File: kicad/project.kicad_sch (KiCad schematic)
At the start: 1 part, among them U1 ESP32-C3-WROOM-02

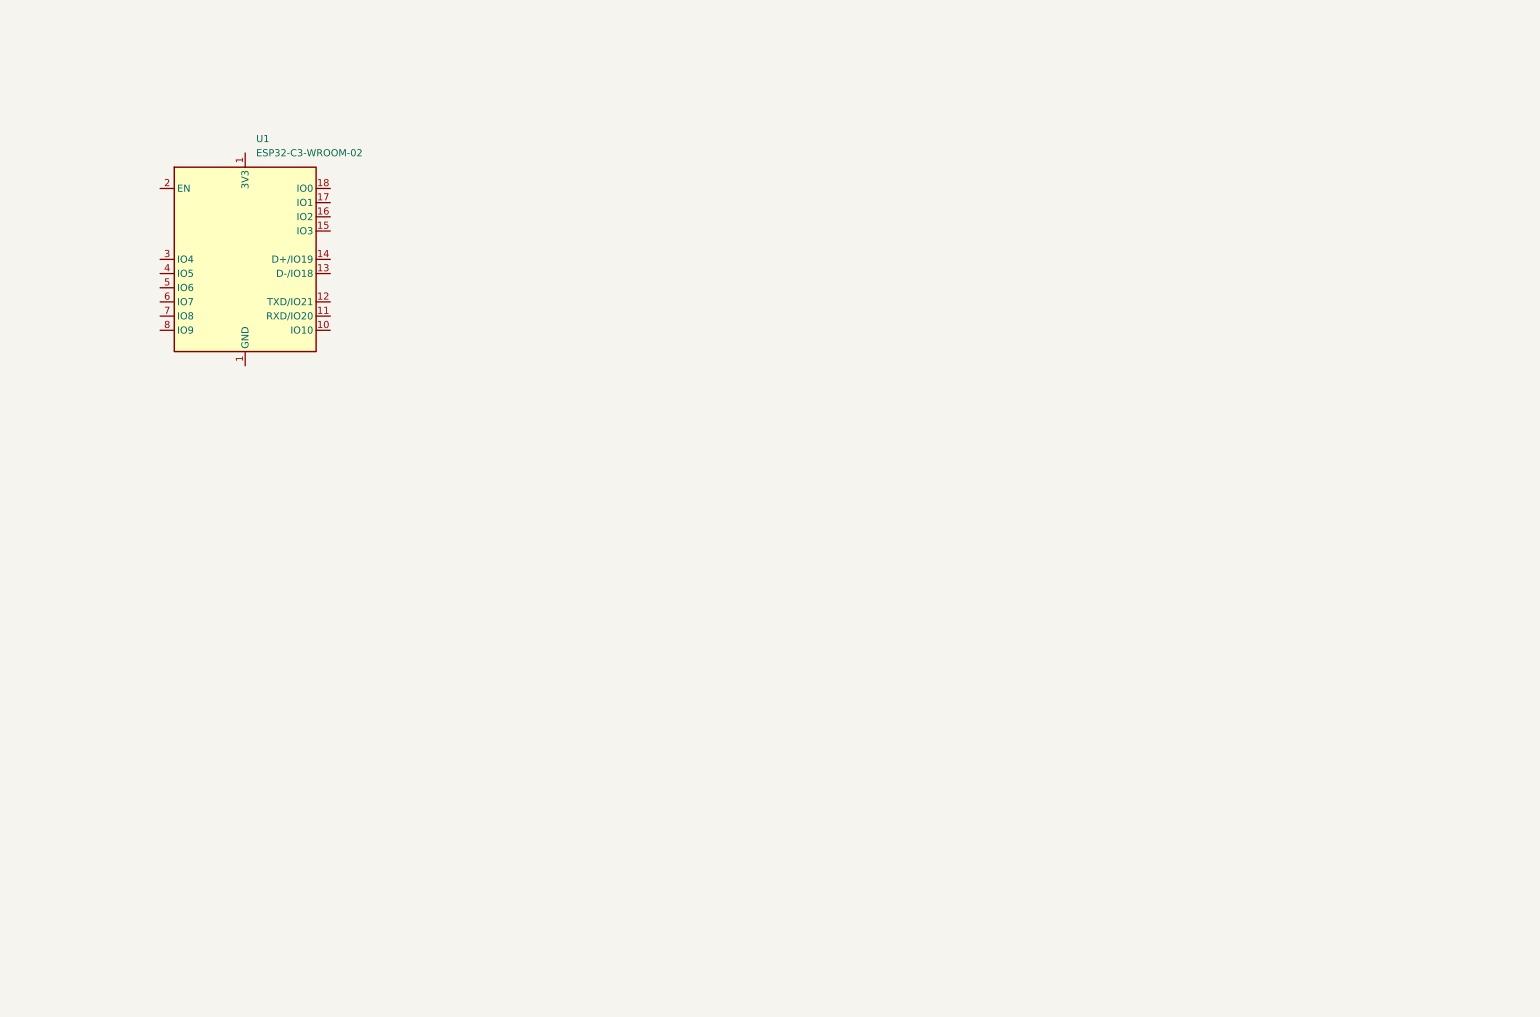
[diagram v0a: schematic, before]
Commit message: Add partial power management circuit
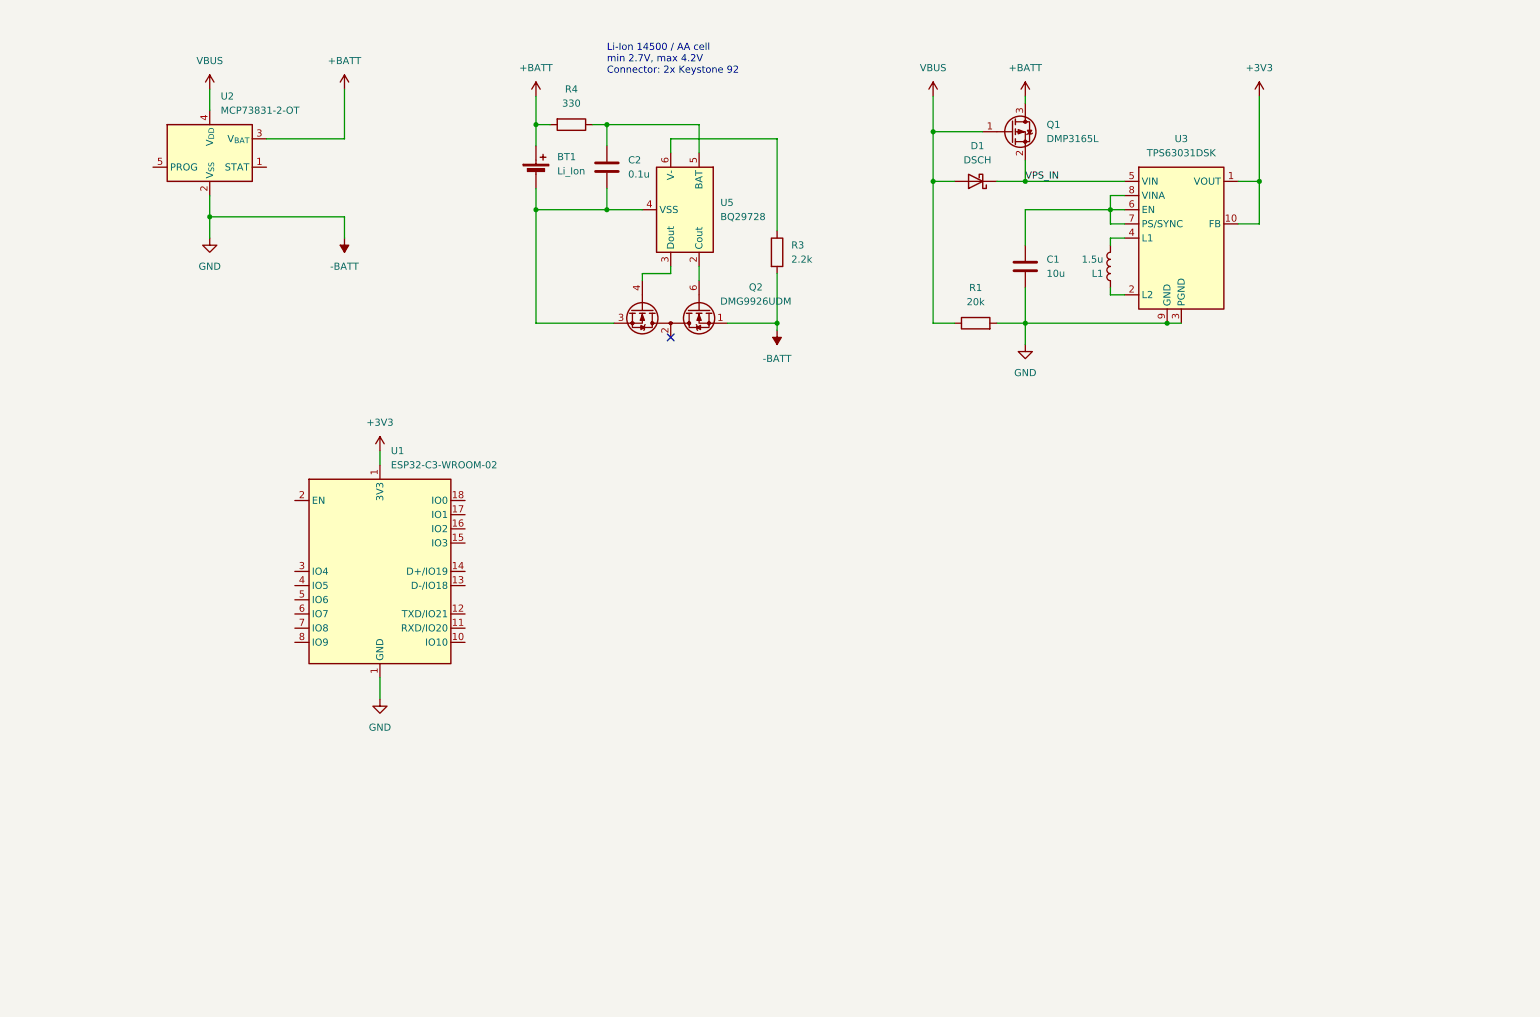
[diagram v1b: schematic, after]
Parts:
- added BT1: Li_Ion, symbol Device:Battery_Cell
- added C1: 10u, symbol Device:C
- added C2: 0.1u, symbol Device:C
- added D1: DSCH, symbol Device:D_Schottky
- added L1: 1.5u, symbol Device:L
- added Q1: DMP3165L, Package_TO_SOT_SMD:SOT-23, symbol Transistor_FET:DMG2301L
- added Q2: DMG9926UDM, Package_TO_SOT_SMD:SOT-23-6, symbol Transistor_FET:DMG9926UDM
- added R1: 20k, symbol Device:R
- added R3: 2.2k, symbol Device:R
- added R4: 330, symbol Device:R
- added U2: MCP73831-2-OT, Package_TO_SOT_SMD:SOT-23-5, symbol Battery_Management:MCP73831-2-OT
- added U3: TPS63031DSK, Package_SON:WSON-10-1EP_2.5x2.5mm_P0.5mm_EP1.2x2mm, symbol Regulator_Switching:TPS63031DSK
- added U5: BQ29728, Package_SON:WSON-6_1.5x1.5mm_P0.5mm, symbol Battery_Management:BQ297xy
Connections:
- net -BATT: now reaches U1.1 (GND)
- net -BATT: now also U1.19 (GND), C1.2, Q2.1 (D1), R1.2, R3.2, U2.2 (V_{SS}), U3.11 (PGND), U3.3 (PGND), U3.9 (GND)
- new net: BT1.2 (-), C2.1, Q2.3 (S2), U5.4 (VSS)
- new net: R3.1, U5.6 (V-)
- new net: L1.1, U3.2 (L2)
- new net: L1.2, U3.4 (L1)
- new net: Q2.6 (G1), U5.2 (Cout)
- new net: Q2.4 (G2), U5.3 (Dout)
- new net: C2.2, R4.1, U5.5 (BAT)
- new net: C1.1, U3.6 (EN), U3.7 (PS/SYNC), U3.8 (VINA)
- new net: Q2.2 (S1/D2), Q2.5 (S1/D2)
- new net +3V3: U1.1 (GND), U3.1 (VOUT), U3.10 (FB)
- new net +BATT: BT1.1 (+), Q1.3 (D), R4.2, U2.3 (V_{BAT})
- new net VBUS: D1.2 (A), Q1.1 (G), R1.1, U2.4 (V_{DD})
- new net VPS_IN: D1.1 (K), Q1.2 (S), U3.5 (VIN)
- no-connect marks 0 -> 1
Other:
- note added: "Li-Ion 14500 / AA cell min 2.7V, max 4.2V Connector: 2x Keystone 92"
- moved on the sheet: U1

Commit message: Add USB-C, update power supply, add initial audio components
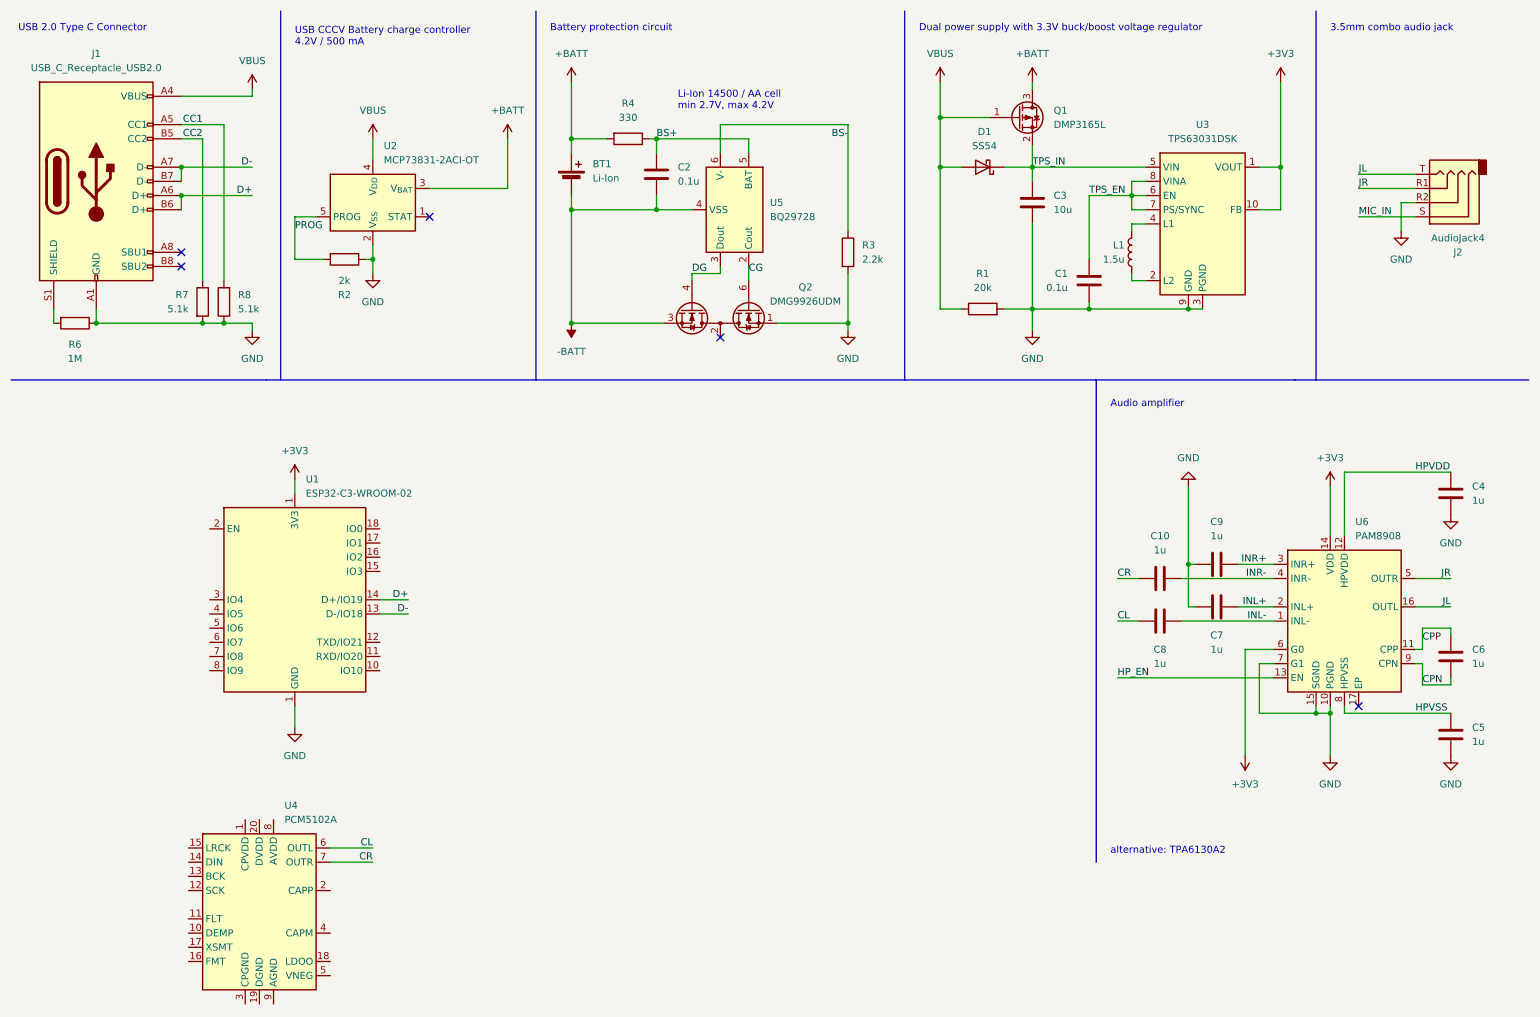
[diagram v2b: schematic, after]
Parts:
- added C10, C4, C5, C6, C7, C8, C9: 1u, Capacitor_SMD:C_0402_1005Metric, symbol Device:C
- added C3: 10u, Capacitor_SMD:C_0402_1005Metric, symbol Device:C
- added J1: USB_C_Receptacle_USB2.0, Connector_USB:USB_C_Receptacle_G-Switch_GT-USB-7010ASV, symbol Connector:USB_C_Receptacle_USB2.0
- added J2: AudioJack4, Connector_Audio:Jack_3.5mm_PJ320D_Horizontal, symbol Connector_Audio:AudioJack4
- added R2: 2k, Resistor_SMD:R_0402_1005Metric, symbol Device:R
- added R6: 1M, Resistor_SMD:R_0402_1005Metric, symbol Device:R
- added R7, R8: 5.1k, Resistor_SMD:R_0402_1005Metric, symbol Device:R
- added U4: PCM5102A, Package_SO:TSSOP-20_4.4x6.5mm_P0.65mm, symbol Audio:PCM5102A
- added U6: PAM8908, Package_DFN_QFN:WQFN-16-1EP_3x3mm_P0.5mm_EP1.6x1.6mm_ThermalVias, symbol Amplifier_Audio:TPA6132A2RTE
- BT1: value Li_Ion -> Li-Ion; footprint (none) -> Battery:BatteryHolder_Keystone_2460_1xAA
- C1: value 10u -> 0.1u; footprint (none) -> Capacitor_SMD:C_0402_1005Metric
- C2: footprint (none) -> Capacitor_SMD:C_0402_1005Metric
- D1: value DSCH -> SS54; footprint (none) -> Diode_SMD:D_SMA
- L1: footprint (none) -> Inductor_SMD:L_1206_3216Metric
- R1, R3, R4: footprint (none) -> Resistor_SMD:R_0402_1005Metric
- U2: value MCP73831-2-OT -> MCP73831-2ACI-OT
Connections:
- net +3V3: now also U6.14 (VDD), U6.6 (G0)
- net -BATT: now also BT1.2 (-), C2.1, Q2.3 (S2), U5.4 (VSS); no longer C1.2, Q2.1 (D1), R1.2, R3.2, U1.1 (GND), U1.19 (GND), U2.2 (V_{SS}), U3.11 (PGND), U3.3 (PGND), U3.9 (GND)
- net VBUS: now also J1.A4 (VBUS), J1.A9 (VBUS), J1.B4 (VBUS), J1.B9 (VBUS)
- net D-: now reaches U1.13 (D-/IO18)
- net D-: now also J1.A7 (D-), J1.B7 (D-)
- net D+: now reaches U1.14 (D+/IO19)
- net D+: now also J1.A6 (D+), J1.B6 (D+)
- net BS-: now reaches R3.1, U5.6 (V-)
- net CG: now reaches Q2.6 (G1), U5.2 (Cout)
- net DG: now reaches Q2.4 (G2), U5.3 (Dout)
- net BS+: now reaches C2.2, R4.1, U5.5 (BAT)
- net TPS_EN: now reaches U3.6 (EN), U3.7 (PS/SYNC), U3.8 (VINA)
- net TPS_EN: now also C1.2; no longer C1.1
- net PROG: now reaches U2.5 (PROG)
- net PROG: now also R2.2
- net VPS_IN renamed TPS_IN
- net TPS_IN: now also C3.1
- new net: J1.S1 (SHIELD), R6.2
- new net CC1: J1.A5 (CC1), R8.2
- new net CC2: J1.B5 (CC2), R7.1
- new net CL: C8.2, U4.6 (OUTL)
- new net CPN: C6.2, U6.9 (CPN)
- new net CPP: C6.1, U6.11 (CPP)
- new net CR: C10.2, U4.7 (OUTR)
- new net GND: C1.1, C3.2, C4.1, C5.1, C7.2, C9.2, J1.A1 (GND), J1.A12 (GND), J1.B1 (GND), J1.B12 (GND), J2.R2, Q2.1 (D1), R1.2, R2.1, R3.2, R6.1, R7.2, R8.1, U1.1 (GND), U1.19 (GND), U2.2 (V_{SS}), U3.11 (PGND), U3.3 (PGND), U3.9 (GND), U6.10 (PGND), U6.15 (SGND), U6.7 (G1)
- new net HPVDD: C4.2, U6.12 (HPVDD)
- new net HPVSS: C5.2, U6.8 (HPVSS)
- new net HP_EN: U6.13 (EN)
- new net INL+: C7.1, U6.2 (INL+)
- new net INL-: C8.1, U6.1 (INL-)
- new net INR+: C9.1, U6.3 (INR+)
- new net INR-: C10.1, U6.4 (INR-)
- new net JL: J2.T, U6.16 (OUTL)
- new net JR: J2.R1, U6.5 (OUTR)
- new net MIC_IN: J2.S
- no-connect marks 1 -> 5
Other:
- note added: "3.5mm combo audio jack"
- note added: "Audio amplifier"
- note added: "Battery protection circuit"
- note added: "Dual power supply with 3.3V buck/boost voltage regulator"
- note added: "Li-Ion 14500 / AA cell min 2.7V, max 4.2V"
- note added: "USB 2.0 Type C Connector"
- note added: "USB CCCV Battery charge controller 4.2V / 500 mA"
- note added: "alternative: TPA6130A2"
- note removed: "Li-Ion 14500 / AA cell min 2.7V, max 4.2V Connector: 2x Keystone 92"
- moved on the sheet: BT1, C1, C2, D1, L1, Q1, Q2, R1, R3, R4, U1, U2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
